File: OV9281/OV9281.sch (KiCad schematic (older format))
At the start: 19 parts, among them IC1 TLV73328PDBVT, IC2 TLV73318PDBVT, IC3 TLV73312PDBVT, J3 WE_68715014522, U1 OV9281, U2 OV9281, Y1 Farnell_1842027, Y2 Farnell_1842027

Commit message: Unified power rails, added power supply filters
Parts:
- added C? (x18): C_1u_0603, antmicro-footprints:0603-cap, symbol antmicro_Capacitors_0603:C_1u_0603
- added C? (x14): C_100n_0402_6V3, antmicro-footprints:0402-cap, symbol antmicro_Capacitors_0402:C_100n_0402_6V3
- added L? (x6): INDUCTOR, symbol pspice:INDUCTOR
- added R? (x12): R_0R_0402, antmicro-footprints:0402-res, symbol antmicro_Resistors_0402:R_0R_0402
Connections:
- net labels added: CAM_RST_1V8, M1_AGND, M1_AVDD, M1_CAM_SCL, M1_CAM_SCL_1V8, M1_CAM_SDA, M1_CAM_SDA_1V8, M1_DGND, M1_DOVDD, M1_DVDD, M1_EVDD, M1_MCLK, M1_PVDD, M1_SID, M1_VH, M1_VN1, M1_VN2, M1_VN3, M1_VSYNC_1V8, M2_AGND, M2_AVDD, M2_CAM_SCL, M2_CAM_SCL_1V8, M2_CAM_SDA, M2_CAM_SDA_1V8, M2_DGND, M2_DOVDD, M2_DVDD, M2_EVDD, M2_MCLK, M2_PVDD, M2_SID, M2_VH, M2_VN1, M2_VN2, M2_VN3, M2_VSYNC_1V8
- net labels removed: AVDD, CAM_L_SCL, CAM_L_SDA, CAM_R_SCL, CAM_R_SDA, CLK_CAM1, CLK_CAM2, CLK_L, CLK_R, DOVDD, DVDD, GNDA, GNDD, PVDD_L, PVDD_P, VH_L, VH_P, VN1_L, VN1_P, VN2_L, VN2_P, VN3_L, VN3_P
- wire segments 254 -> 354
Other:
- note added: "TODO: add level shifting for all IO/s to 3v3 and invert SHUTDOWN signal"
- note added: "analog and digital grounds connected in signle point"
- note added: "slave addr select"
- moved on the sheet: C1, C2, C3, C4, C5, C6, IC1, IC2, IC3, J3, R1, R2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

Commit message: Added voltage level translation
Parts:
- added Q?: BSS138, antmicro-footprints:SOT-23-3, symbol antmicro_Transistors_FETs_MOSFETs_Single:BSS138
- added R?: R_10k_0402, antmicro-footprints:0402-res, symbol antmicro_Resistors_0402:R_10k_0402
- added R?: R_2k_0402, antmicro-footprints:0402-res, symbol antmicro_Resistors_0402:R_2k_0402
- added U?: NTS0104BQ, antmicro-footprints:QDHVQFN14, symbol antmicro_Logic_Translators_Level_Shifters:NTS0104BQ
- added U?: NTB0104BQ, antmicro-footprints:QDHVQFN14, symbol antmicro_Logic_Translators_Level_Shifters:NTB0104BQ
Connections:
- net labels added: CAM_NRST_1V8, M1_VSYNC, M2_VSYNC
- net labels removed: VSYNC_1, VSYNC_2
- wire segments 354 -> 391
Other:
- note added: "Shutdown negation"
- note added: "Voltage Level Translation"
- note removed: "TODO: add level shifting for all IO/s to 3v3 and invert SHUTDOWN signal"
- moved on the sheet: C?, Y1, Y2

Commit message: Updated transistor and inductors from libraries
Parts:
- removed L? (x6): INDUCTOR, symbol pspice:INDUCTOR
- removed Q?: BSS138, antmicro-footprints:SOT-23-3, symbol antmicro_Transistors_FETs_MOSFETs_Single:BSS138
- added L1, L2, L3, L4, L5, L6: MLP2012S3R3MT, antmicro-footprints:0805-res, symbol antmicro_Fixed_Inductors:MLP2012S3R3MT
- added Q1: BSS138AKA, antmicro-footprints:SOT-23-3, symbol antmicro_Transistors_FETs_MOSFETs_Single:BSS138AKA
- added R? (x2): R_0R_0402, antmicro-footprints:0402-res, symbol antmicro_Resistors_0402:R_0R_0402
- gave numbers to parts that had none: 48
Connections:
- net labels added: M2_MCLK_M
- wire segments 391 -> 396
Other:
- note added: "DNP"

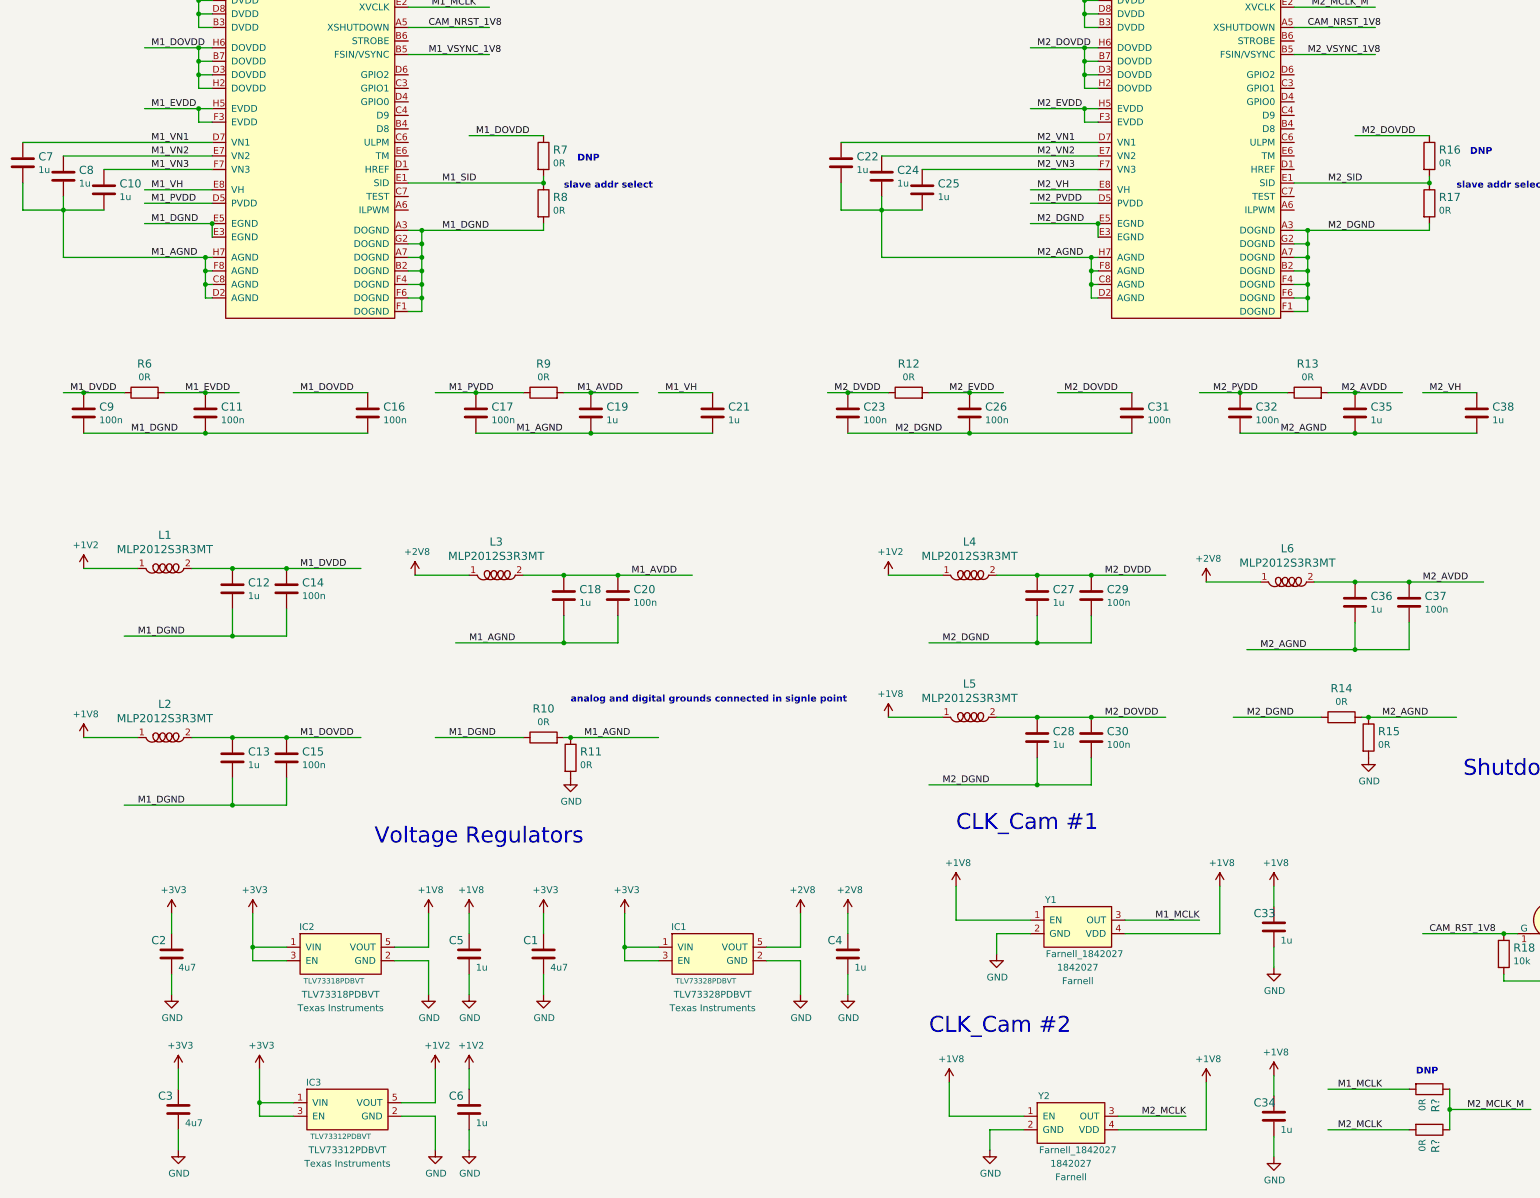
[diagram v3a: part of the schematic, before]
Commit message: Edited design rules to make bigger clearance
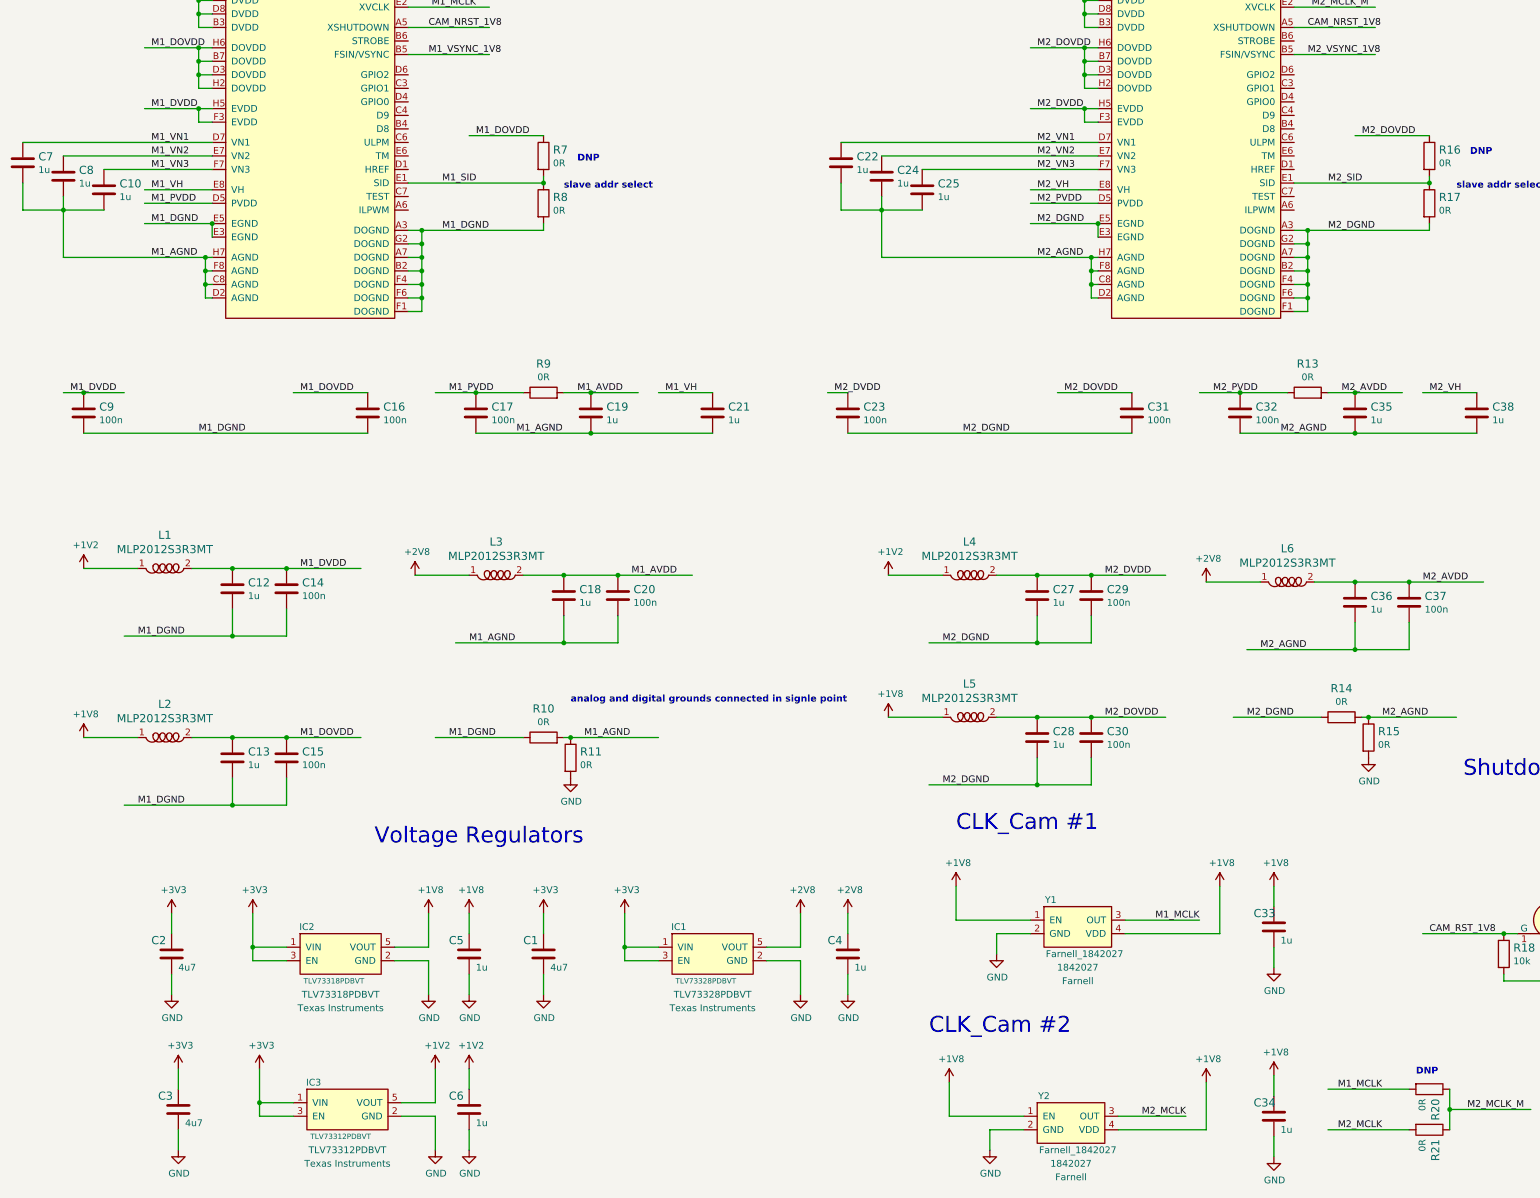
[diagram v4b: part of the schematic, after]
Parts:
- removed C11, C26: C_100n_0402_6V3, antmicro-footprints:0402-cap, symbol antmicro_Capacitors_0402:C_100n_0402_6V3
- removed R12, R6: R_0R_0402, antmicro-footprints:0402-res, symbol antmicro_Resistors_0402:R_0R_0402
- gave numbers to parts that had none: 2
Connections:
- net labels removed: M1_EVDD, M2_EVDD
- wire segments 396 -> 389
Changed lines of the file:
@@
 	8450 2850 8450 2750
 Connection ~ 8450 2750
-Text Label 1550 3000 0    50   ~ 0
-M1_EVDD
-Text Label 8100 3000 0    50   ~ 0
-M2_EVDD
 $Comp
 L antmicro_Image_Sensors:OV9281 U2
@@
 Text Label 950  5100 0    50   ~ 0
 M1_DVDD
-Text Label 1800 5100 0    50   ~ 0
-M1_EVDD
-$Comp
-L antmicro_Resistors_0402:R_0R_0402 R6
-U 1 1 5DB82014
-P 1500 5100
-F 0 "R6" H 1500 5313 60  0000 C CNN
-F 1 "R_0R_0402" H 1500 4950 60  0001 C CNN
-F 2 "antmicro-footprints:0402-res" H 1700 5300 60  0001 L CNN
-F 3 "" H 1500 5100 50  0001 C CNN
-F 4 "PANASONIC" H 1700 5500 60  0001 L CNN "Manufacturer"
-F 5 "ERJ2GE0R00X" H 1700 5400 60  0001 L CNN "MPN"
-F 6 "0R" H 1500 5215 50  0000 C CNN "Val"
-	1    1500 5100
-	1    0    0    -1
-$EndComp
 Wire Wire Line
 	1350 5100 1050 5100
-Wire Wire Line
-	1650 5100 1950 5100
 Wire Wire Line
 	2600 5100 3150 5100
@@
 Wire Wire Line
 	1050 5100 900  5100
-$Comp
-L antmicro_Capacitors_0402:C_100n_0402_6V3 C11
-U 1 1 5DBD8EA4
-P 1950 5250
-F 0 "C11" H 2065 5295 60  0000 L CNN
-F 1 "C_100n_0402_6V3" H 1950 5100 60  0001 C CNN
-F 2 "antmicro-footprints:0402-cap" H 2150 5450 60  0001 L CNN
-F 3 "" H 1950 5250 50  0001 C CNN
-F 4 "Walsin" H 2150 5650 60  0001 L CNN "Manufacturer"
-F 5 "0402X104K6R3CT" H 2150 5550 60  0001 L CNN "MPN"
-F 6 "100n" H 2065 5197 50  0000 L CNN "Val"
-	1    1950 5250
-	1    0    0    -1
-$EndComp
-Connection ~ 1950 5100
-Wire Wire Line
-	1950 5100 2200 5100
-Wire Wire Line
-	1050 5400 1950 5400
-Text Label 1400 5400 0    50   ~ 0
+Text Label 1900 5400 0    50   ~ 0
 M1_DGND
 Text Label 2650 5100 0    50   ~ 0
@@
 $EndComp
 Wire Wire Line
-	3150 5400 1950 5400
-Connection ~ 1950 5400
-Wire Wire Line
 	3650 5100 3950 5100
 Text Label 3750 5100 0    50   ~ 0
@@
 Text Label 6600 5100 0    50   ~ 0
 M2_DVDD
-Text Label 7450 5100 0    50   ~ 0
-M2_EVDD
-$Comp
-L antmicro_Resistors_0402:R_0R_0402 R12
-U 1 1 5DE3E7C4
-P 7150 5100
-F 0 "R12" H 7150 5313 60  0000 C CNN
-F 1 "R_0R_0402" H 7150 4950 60  0001 C CNN
-F 2 "antmicro-footprints:0402-res" H 7350 5300 60  0001 L CNN
-F 3 "" H 7150 5100 50  0001 C CNN
-F 4 "PANASONIC" H 7350 5500 60  0001 L CNN "Manufacturer"
-F 5 "ERJ2GE0R00X" H 7350 5400 60  0001 L CNN "MPN"
-F 6 "0R" H 7150 5215 50  0000 C CNN "Val"
-	1    7150 5100
-	1    0    0    -1
-$EndComp
-Wire Wire Line
-	7000 5100 6700 5100
-Wire Wire Line
-	7300 5100 7600 5100
 Wire Wire Line
 	8250 5100 8800 5100
@@
 	1    0    0    -1
 $EndComp
-Connection ~ 6700 5100
 Wire Wire Line
 	6700 5100 6550 5100
-$Comp
-L antmicro_Capacitors_0402:C_100n_0402_6V3 C26
-U 1 1 5DE3E7DD
-P 7600 5250
-F 0 "C26" H 7715 5295 60  0000 L CNN
-F 1 "C_100n_0402_6V3" H 7600 5100 60  0001 C CNN
-F 2 "antmicro-footprints:0402-cap" H 7800 5450 60  0001 L CNN
-F 3 "" H 7600 5250 50  0001 C CNN
-F 4 "Walsin" H 7800 5650 60  0001 L CNN "Manufacturer"
-F 5 "0402X104K6R3CT" H 7800 5550 60  0001 L CNN "MPN"
-F 6 "100n" H 7715 5197 50  0000 L CNN "Val"
-	1    7600 5250
-	1    0    0    -1
-$EndComp
-Connection ~ 7600 5100
-Wire Wire Line
-	7600 5100 7850 5100
-Wire Wire Line
-	6700 5400 7600 5400
-Text Label 7050 5400 0    50   ~ 0
+Text Label 7550 5400 0    50   ~ 0
 M2_DGND
 Text Label 8300 5100 0    50   ~ 0
@@
 	1    0    0    -1
 $EndComp
-Wire Wire Line
-	8800 5400 7600 5400
-Connection ~ 7600 5400
 Wire Wire Line
 	9300 5100 9600 5100
@@
 $EndComp
 $Comp
-L antmicro_Resistors_0402:R_0R_0402 R?
+L antmicro_Resistors_0402:R_0R_0402 R20
 U 1 1 5D94152F
 P 11000 10250
-F 0 "R?" V 10955 10320 60  0000 L CNN
+F 0 "R20" V 10955 10320 60  0000 L CNN
 F 1 "R_0R_0402" H 11000 10100 60  0001 C CNN
 F 2 "antmicro-footprints:0402-res" H 11200 10450 60  0001 L CNN
@@
 $EndComp
 $Comp
-L antmicro_Resistors_0402:R_0R_0402 R?
+L antmicro_Resistors_0402:R_0R_0402 R21
 U 1 1 5D941653
 P 11000 10550
-F 0 "R?" V 10955 10620 60  0000 L CNN
+F 0 "R21" V 10955 10620 60  0000 L CNN
 F 1 "R_0R_0402" H 11000 10400 60  0001 C CNN
 F 2 "antmicro-footprints:0402-res" H 11200 10750 60  0001 L CNN
@@
 Wire Notes Line
 	13850 4050 13850 4800
+Wire Wire Line
+	1050 5400 3150 5400
+Wire Wire Line
+	6700 5400 8800 5400
+Text Label 1550 3000 0    50   ~ 0
+M1_DVDD
+Text Label 8100 3000 0    50   ~ 0
+M2_DVDD
 $EndSCHEMATC

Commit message: PCB ready for manufacturing
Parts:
- added MP1, MP2, MP3, MP4: PCB_Spacer_M2, antmicro-footprints:9774030243R, symbol OV9281-rescue:PCB_Spacer_M2-antmicro_Mechanical_Parts
- added N1: antmicro_logo, antmicro-footprints:antmicro-logo_scaled_20mm, symbol OV9281-rescue:antmicro_logo-antmicro_Mechanical_Parts
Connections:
- wire segments 389 -> 393
- no-connect marks 0 -> 47
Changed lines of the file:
@@
 Text Label 8100 3000 0    50   ~ 0
 M2_DVDD
+$Comp
+L OV9281-rescue:PCB_Spacer_M2-antmicro_Mechanical_Parts MP3
+U 1 1 5D8EFB53
+P 12000 6450
+F 0 "MP3" H 12208 6587 50  0000 L CNN
+F 1 "PCB_Spacer_M2" H 12208 6496 50  0000 L CNN
+F 2 "antmicro-footprints:9774030243R" H 12800 7150 50  0001 C CNN
+F 3 "https://katalog.we-online.de/em/datasheet/9774030243R.pdf" H 12950 7250 50  0001 C CNN
+F 4 "9774030243R" H 12208 6405 50  0000 L CNN "MPN"
+F 5 "Wurth Elektronik " H 12208 6314 50  0000 L CNN "Manufacturer"
+	1    12000 6450
+	1    0    0    -1
+$EndComp
+$Comp
+L OV9281-rescue:PCB_Spacer_M2-antmicro_Mechanical_Parts MP4
+U 1 1 5D8F000C
+P 12000 7000
+F 0 "MP4" H 12208 7137 50  0000 L CNN
+F 1 "PCB_Spacer_M2" H 12208 7046 50  0000 L CNN
+F 2 "antmicro-footprints:9774030243R" H 12800 7700 50  0001 C CNN
+F 3 "https://katalog.we-online.de/em/datasheet/9774030243R.pdf" H 12950 7800 50  0001 C CNN
+F 4 "9774030243R" H 12208 6955 50  0000 L CNN "MPN"
+F 5 "Wurth Elektronik " H 12208 6864 50  0000 L CNN "Manufacturer"
+	1    12000 7000
+	1    0    0    -1
+$EndComp
+$Comp
+L OV9281-rescue:PCB_Spacer_M2-antmicro_Mechanical_Parts MP2
+U 1 1 5D91C3CF
+P 12000 5900
+F 0 "MP2" H 12208 6037 50  0000 L CNN
+F 1 "PCB_Spacer_M2" H 12208 5946 50  0000 L CNN
+F 2 "antmicro-footprints:9774030243R" H 12800 6600 50  0001 C CNN
+F 3 "https://katalog.we-online.de/em/datasheet/9774030243R.pdf" H 12950 6700 50  0001 C CNN
+F 4 "9774030243R" H 12208 5855 50  0000 L CNN "MPN"
+F 5 "Wurth Elektronik " H 12208 5764 50  0000 L CNN "Manufacturer"
+	1    12000 5900
+	1    0    0    -1
+$EndComp
+$Comp
+L OV9281-rescue:PCB_Spacer_M2-antmicro_Mechanical_Parts MP1
+U 1 1 5D948FB2
+P 12000 5400
+F 0 "MP1" H 12208 5537 50  0000 L CNN
+F 1 "PCB_Spacer_M2" H 12208 5446 50  0000 L CNN
+F 2 "antmicro-footprints:9774030243R" H 12800 6100 50  0001 C CNN
+F 3 "https://katalog.we-online.de/em/datasheet/9774030243R.pdf" H 12950 6200 50  0001 C CNN
+F 4 "9774030243R" H 12208 5355 50  0000 L CNN "MPN"
+F 5 "Wurth Elektronik " H 12208 5264 50  0000 L CNN "Manufacturer"
+	1    12000 5400
+	1    0    0    -1
+$EndComp
+$Comp
+L OV9281-rescue:antmicro_logo-antmicro_Mechanical_Parts N1
+U 1 1 5D9A49D0
+P 5350 10750
+F 0 "N1" H 5400 11103 50  0000 C CNN
+F 1 "antmicro_logo" H 5400 11012 50  0000 C CNN
+F 2 "antmicro-footprints:antmicro-logo_scaled_20mm" H 5250 11000 50  0001 C CNN
+F 3 "" H 5350 11100 50  0001 C CNN
+	1    5350 10750
+	1    0    0    -1
+$EndComp
+NoConn ~ 3450 2150
+NoConn ~ 3450 2500
+NoConn ~ 3450 2750
+NoConn ~ 3450 2850
+NoConn ~ 3450 2950
+NoConn ~ 3450 3050
+NoConn ~ 3450 3150
+NoConn ~ 3450 3250
+NoConn ~ 3450 3450
+NoConn ~ 3450 3650
+NoConn ~ 3450 3750
+NoConn ~ 10000 2150
+NoConn ~ 10000 2500
+NoConn ~ 10000 2750
+NoConn ~ 10000 2850
+NoConn ~ 10000 2950
+NoConn ~ 10000 3050
+NoConn ~ 10000 3150
+NoConn ~ 10000 3250
+NoConn ~ 10000 3450
+NoConn ~ 10000 3650
+NoConn ~ 10000 3750
+NoConn ~ 14600 1000
+NoConn ~ 14600 1100
+NoConn ~ 14600 1200
+NoConn ~ 14600 1300
+NoConn ~ 14600 2200
+NoConn ~ 14600 2300
+NoConn ~ 14600 2500
+NoConn ~ 14600 2600
+NoConn ~ 14600 2800
+NoConn ~ 14600 2900
+NoConn ~ 14600 3000
+NoConn ~ 14600 3100
+NoConn ~ 14600 4000
+NoConn ~ 14600 4400
+NoConn ~ 14600 4500
+NoConn ~ 14600 4600
+NoConn ~ 14600 4700
+NoConn ~ 14600 5200
+NoConn ~ 14600 5300
+NoConn ~ 14600 5400
+NoConn ~ 14600 5500
+NoConn ~ 14600 5800
+NoConn ~ 14600 5900
+NoConn ~ 14000 9300
+NoConn ~ 14800 9300
+Wire Wire Line
+	3450 3350 3550 3350
+Wire Wire Line
+	3550 3350 3550 3900
+Wire Wire Line
+	10000 3350 10100 3350
+Wire Wire Line
+	10100 3350 10100 3900
 $EndSCHEMATC
